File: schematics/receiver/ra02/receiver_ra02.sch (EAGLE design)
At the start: 47 parts, among them IC1 ATMEGA328P, Q1 16MHz, Q2 BC817-16SMD, U1 RFM95_LORA_MODULE, U2 AMS1117_3.3

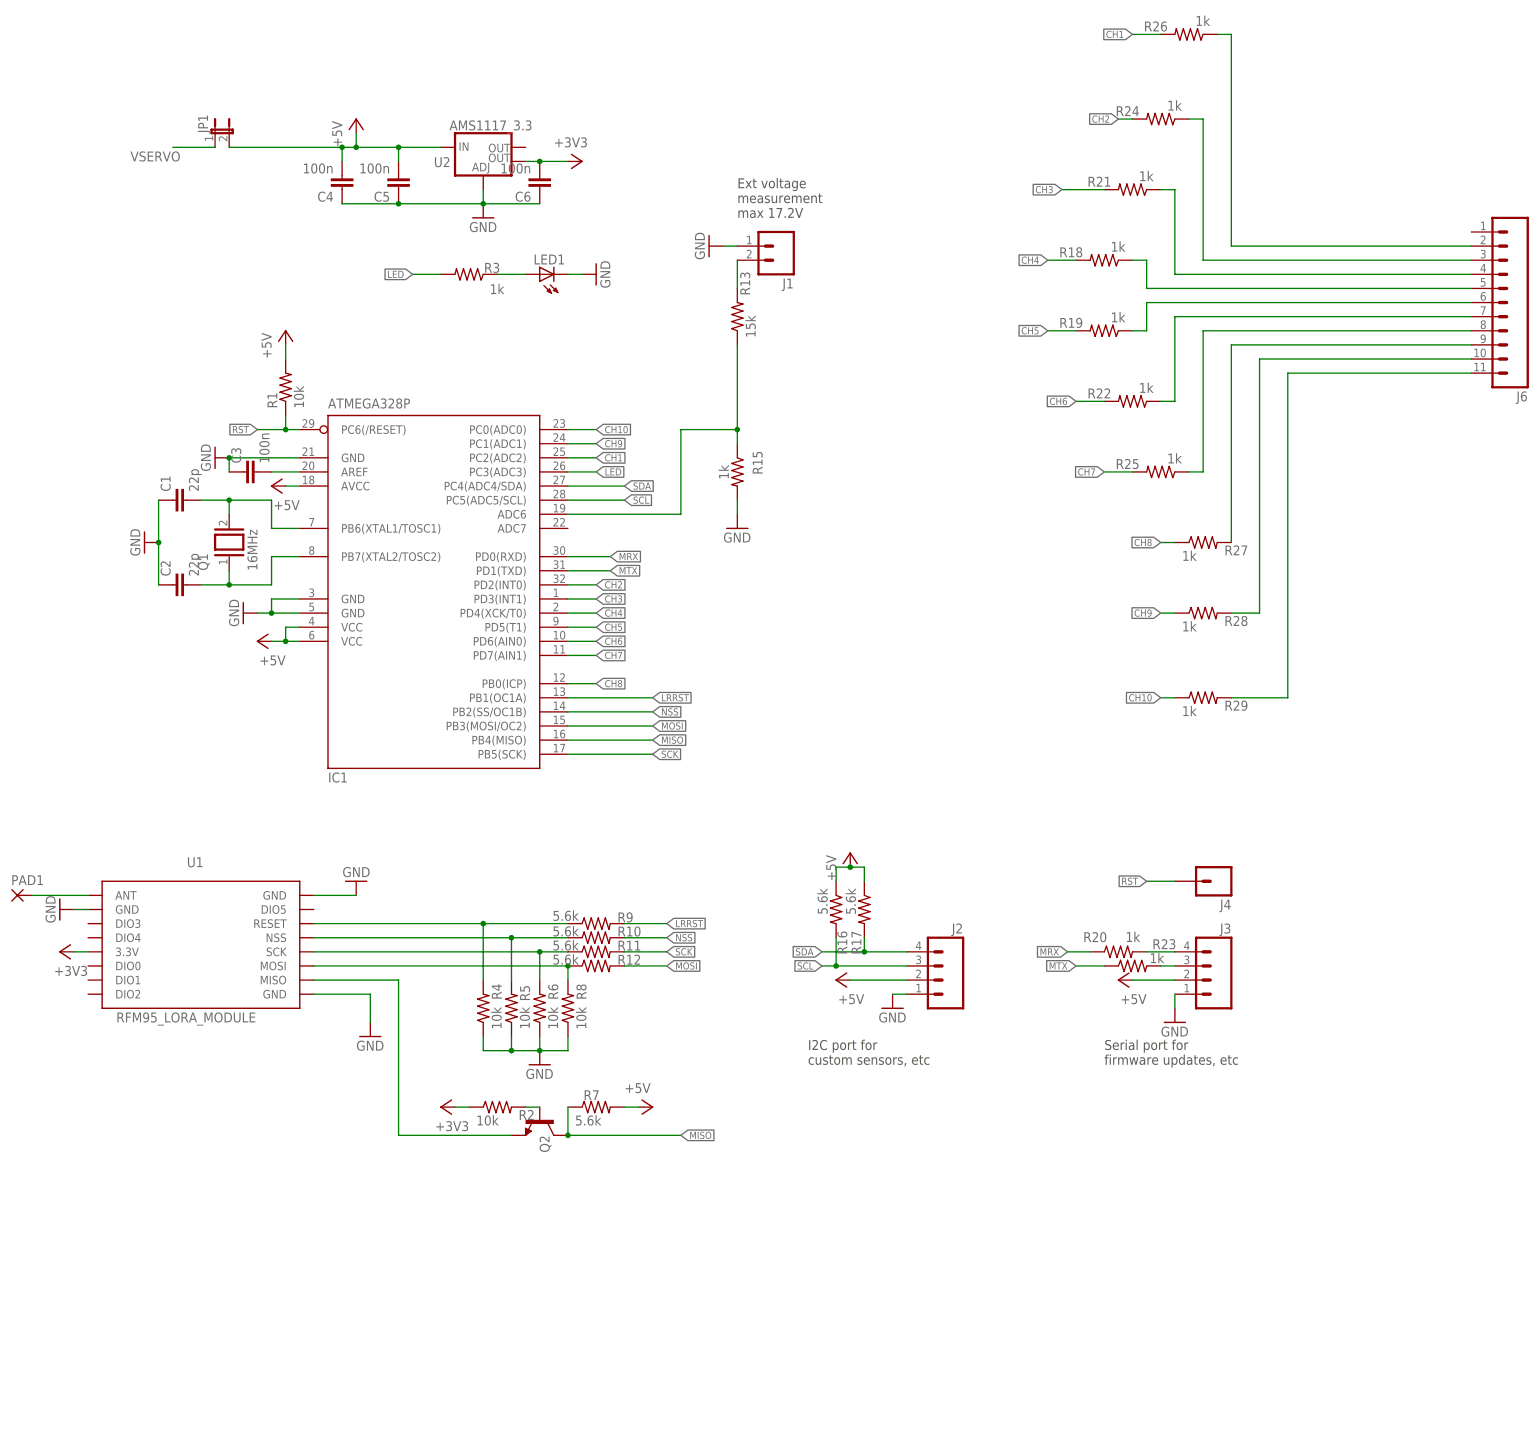
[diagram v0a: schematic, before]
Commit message: Enhancements: ST7920 LCD Support, Documentation and schematics updates, minor fixes and improvements. (#51)
* Update readme.md

* Delete assets/Bm437_Portfolio_6x8_modBUK.FON

* Add files via upload

* Update readme.txt

* Update readme.txt

* Add files via upload

* Delete schematics directory

* Add files via upload

* Update config.h

Added support for ST7920 based LCD.

* Update font.cpp

Added support for ST7920 based LCD.

* Update ui_128x64.cpp

- Added support for ST7920 based LCD.
- Fixed minor bug in when showing tool-tip in mixer monitor screen, when the output is none.
- Other minor improvements.

* Update sdStore.cpp

- Added support for ST7920 LCD.
- Other minor improvements.

* Update font.h

Added support for ST7920 LCD.

* Update ui.h

Added support for ST7920 LCD.

* Add files via upload

Added support for ST7920 LCD.

* Update config.h

* Update receiver.cpp

* Update rfComm.cpp

* Add files via upload

* Update README.md

* Update config.h

Bump version number.

* Add files via upload
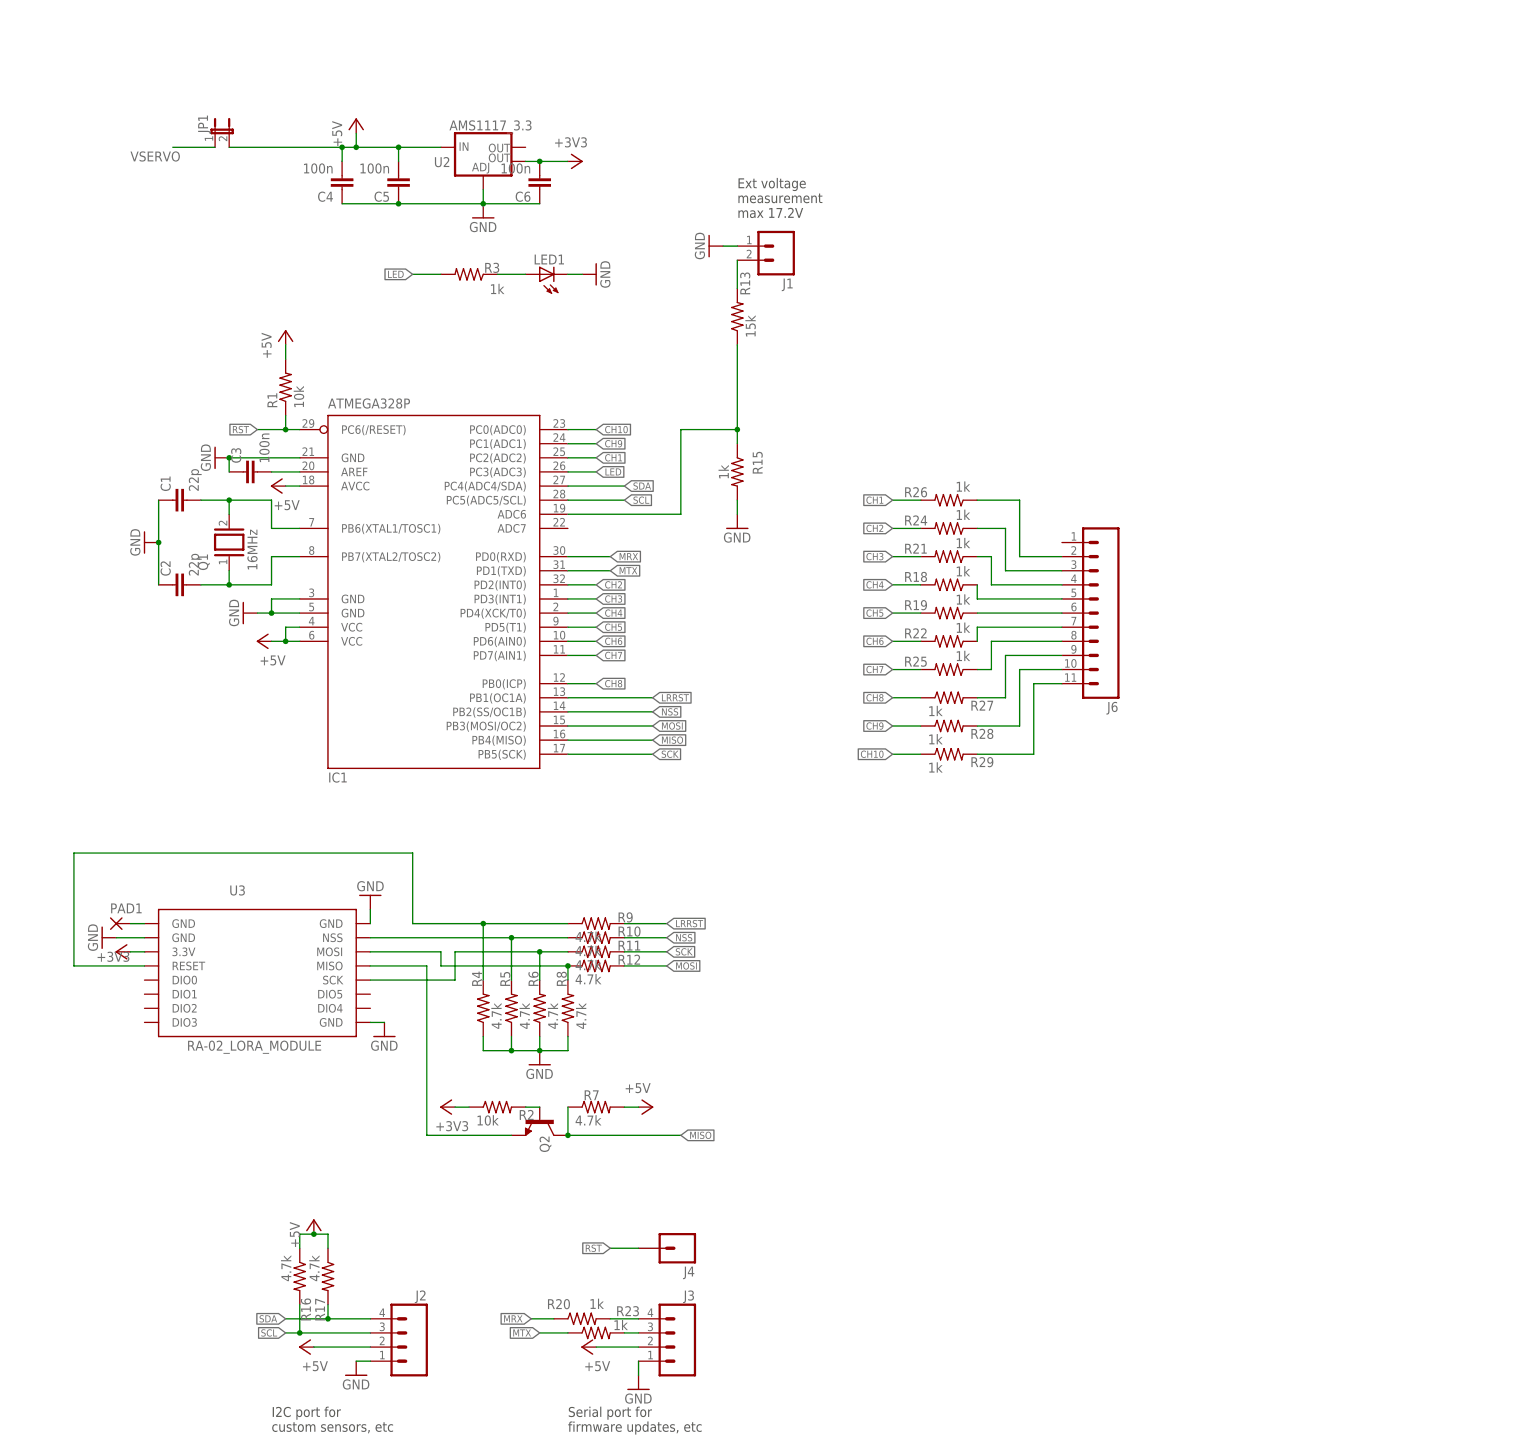
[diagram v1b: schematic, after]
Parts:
- removed U1: RFM95_LORA_MODULE, RFM95_Lora_module:RFM95_LORA_MODULE
- added U3: RA-02_LORA_MODULE, RA-02_Lora_module:RA-02_LORA_MODULE
- R10, R11, R12, R16, R17, R7, R9: value 5.6k -> 4.7k
- R4, R5, R6, R8: value 10k -> 4.7k
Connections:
- removed net N$17: PAD1.P, U1.ANT
- new net N$5: PAD1.P, U3.GND
- net +3V3: now also U3.3.3V; no longer U1.3.3V
- net GND: now also U3.GND@2, U3.GND@3, U3.GND@4; no longer U1.GND, U1.GND@1, U1.GND@2
- net N$11: now also U3.MISO; no longer U1.MISO
- net N$6: now also U3.RESET; no longer U1.RESET
- net N$7: now also U3.NSS; no longer U1.NSS
- net N$8: now also U3.SCK; no longer U1.SCK
- net N$9: now also U3.MOSI; no longer U1.MOSI
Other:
- moved on the sheet: J2, J3, J4, J6, PAD1, R16, R17, R18, R19, R20, R21, R22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
